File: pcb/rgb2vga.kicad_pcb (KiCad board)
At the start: 2 copper layers, 70.5 x 55.9 mm, 41 parts, among them J1 GPIO_0, J2 RGB_IN, J3 COCO3_RGB_IN, J4 C_VIDEO_IN, J5 GPIO_1, J6 VGA_OUT, J7 Conn_01x03_Male, SW1 SW_DIP_x10, SW2 SW_DP3T, U1 LM1881

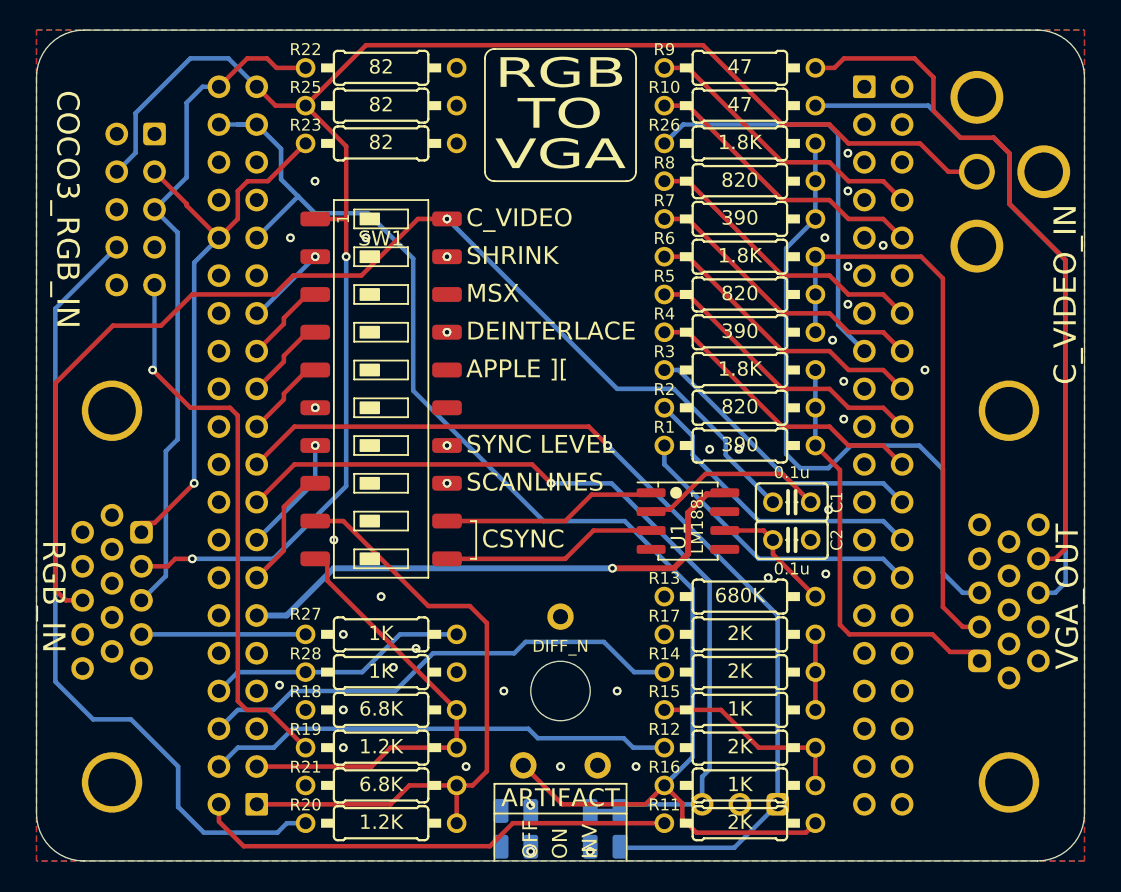
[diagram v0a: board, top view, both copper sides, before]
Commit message: multi-turn DAC trimmer pot
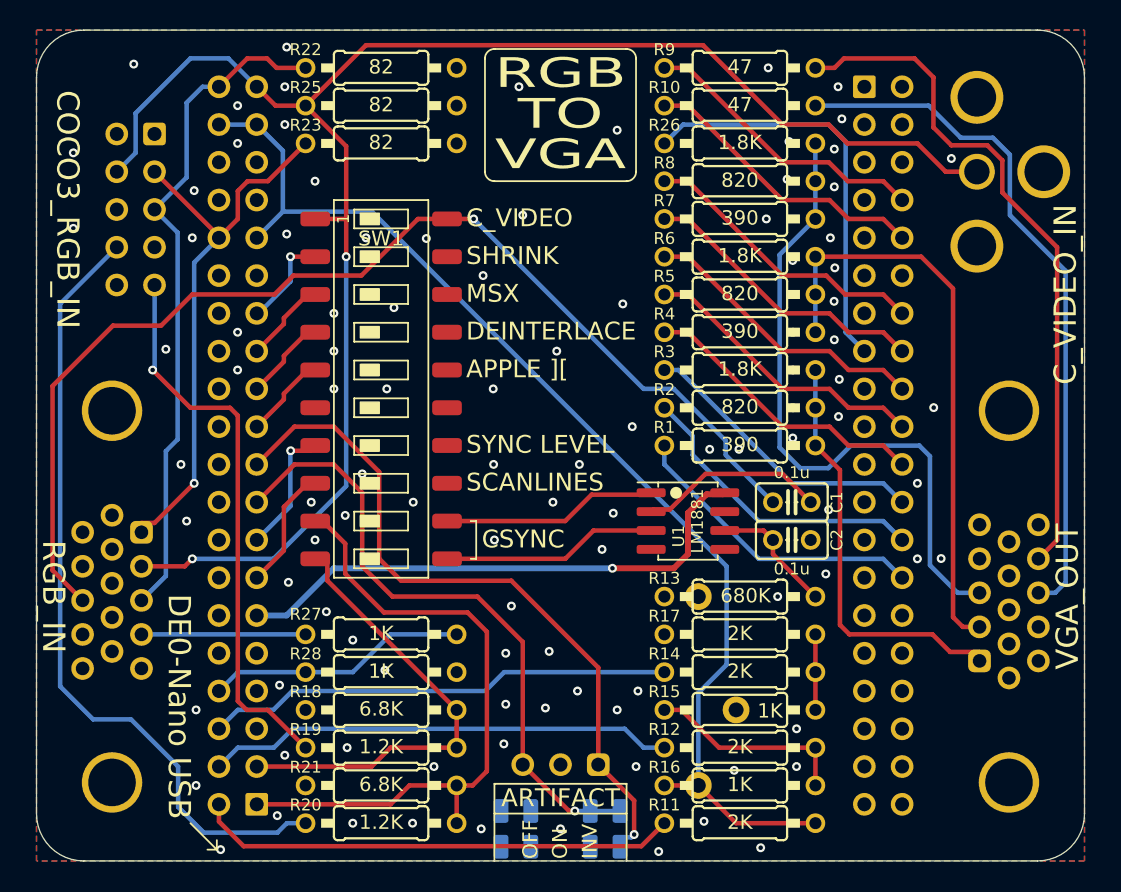
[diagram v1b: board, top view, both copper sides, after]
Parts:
- R24: footprint 000_LOCAL:PT10Lx-hole -> 000_LOCAL:Potentiometer_Bourns_3006P_Horizontal
- moved J7 12.4 mm to (145.7, 122.4)
- moved R24 11.2 mm to (152.5, 111.1), turned to 90 degrees
- renumbered REF** to DE0-Nano
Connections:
- J1 pad 10: (no net) -> unconnected-(J1-Pin_10-Pad10)
- J1 pad 14: (no net) -> unconnected-(J1-Pin_14-Pad14)
- J1 pad 16: (no net) -> unconnected-(J1-Pin_16-Pad16)
- J1 pad 18: (no net) -> unconnected-(J1-Pin_18-Pad18)
- J1 pad 20: (no net) -> unconnected-(J1-Pin_20-Pad20)
- J1 pad 22: (no net) -> unconnected-(J1-Pin_22-Pad22)
- J1 pad 24: (no net) -> unconnected-(J1-Pin_24-Pad24)
- J1 pad 26: (no net) -> unconnected-(J1-Pin_26-Pad26)
- J1 pad 28: (no net) -> unconnected-(J1-Pin_28-Pad28)
- J1 pad 29: (no net) -> unconnected-(J1-Pin_29-Pad29)
- J1 pad 33: (no net) -> unconnected-(J1-Pin_33-Pad33)
- J1 pad 34: (no net) -> unconnected-(J1-Pin_34-Pad34)
- J1 pad 35: (no net) -> unconnected-(J1-Pin_35-Pad35)
- J1 pad 36: (no net) -> unconnected-(J1-Pin_36-Pad36)
- J1 pad 5: (no net) -> unconnected-(J1-Pin_5-Pad5)
- J1 pad 7: (no net) -> unconnected-(J1-Pin_7-Pad7)
- J1 pad 9: (no net) -> unconnected-(J1-Pin_9-Pad9)
- J2 pad 11: (no net) -> unconnected-(J2-Pad11)
- J2 pad 12: (no net) -> unconnected-(J2-Pad12)
- J2 pad 14: (no net) -> unconnected-(J2-Pad14)
- J2 pad 15: (no net) -> unconnected-(J2-Pad15)
- J3 pad 6: (no net) -> unconnected-(J3-Pin_6-Pad6)
- J3 pad 7: (no net) -> unconnected-(J3-Pin_7-Pad7)
- J5 pad 1: (no net) -> unconnected-(J5-Pin_1-Pad1)
- J5 pad 11: (no net) -> unconnected-(J5-Pin_11-Pad11)
- J5 pad 13: (no net) -> unconnected-(J5-Pin_13-Pad13)
- J5 pad 17: (no net) -> unconnected-(J5-Pin_17-Pad17)
- J5 pad 19: (no net) -> unconnected-(J5-Pin_19-Pad19)
- J5 pad 2: (no net) -> unconnected-(J5-Pin_2-Pad2)
- J5 pad 21: (no net) -> unconnected-(J5-Pin_21-Pad21)
- J5 pad 23: (no net) -> unconnected-(J5-Pin_23-Pad23)
- J5 pad 25: (no net) -> unconnected-(J5-Pin_25-Pad25)
- J5 pad 27: (no net) -> unconnected-(J5-Pin_27-Pad27)
- J5 pad 29: (no net) -> unconnected-(J5-Pin_29-Pad29)
- J5 pad 3: (no net) -> unconnected-(J5-Pin_3-Pad3)
- J5 pad 31: (no net) -> unconnected-(J5-Pin_31-Pad31)
- J5 pad 32: (no net) -> unconnected-(J5-Pin_32-Pad32)
- J5 pad 33: (no net) -> unconnected-(J5-Pin_33-Pad33)
- J5 pad 34: (no net) -> unconnected-(J5-Pin_34-Pad34)
- J5 pad 35: (no net) -> unconnected-(J5-Pin_35-Pad35)
- J5 pad 36: (no net) -> unconnected-(J5-Pin_36-Pad36)
- J5 pad 37: (no net) -> unconnected-(J5-Pin_37-Pad37)
- J5 pad 38: (no net) -> unconnected-(J5-Pin_38-Pad38)
- J5 pad 39: (no net) -> unconnected-(J5-Pin_39-Pad39)
- J5 pad 4: (no net) -> unconnected-(J5-Pin_4-Pad4)
- J5 pad 40: (no net) -> unconnected-(J5-Pin_40-Pad40)
- J5 pad 5: (no net) -> unconnected-(J5-Pin_5-Pad5)
- J5 pad 6: (no net) -> unconnected-(J5-Pin_6-Pad6)
- J5 pad 7: (no net) -> unconnected-(J5-Pin_7-Pad7)
- J5 pad 9: (no net) -> unconnected-(J5-Pin_9-Pad9)
- J6 pad 11: (no net) -> unconnected-(J6-Pad11)
- J6 pad 12: (no net) -> unconnected-(J6-Pad12)
- J6 pad 15: (no net) -> unconnected-(J6-Pad15)
- J6 pad 4: (no net) -> unconnected-(J6-Pad4)
- R24 pad 1: (no net) -> GND
- U1 pad 5: (no net) -> unconnected-(U1-BURST-Pad5)
- U1 pad 7: (no net) -> unconnected-(U1-O/E-Pad7)
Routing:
- net /SW_ARTIF_INV: track 65.9 -> 48.0 mm
- net /DIFF_N: track 93.9 -> 78.1 mm
- net /SW_ARTIFACT: track 57.7 -> 42.9 mm
- net /D0: track 33.2 -> 31.5 mm
- net /VGA_V: track 47.5 -> 46.5 mm
- net /SW_SHRINK: track 5.51 -> 6.49 mm
- net /_HSYNC: track 43.3 -> 44.1 mm
- net /SW_SYNC_LVL: track 7.98 -> 8.74 mm
- net /VGA_B: track 43.9 -> 44.5 mm
- net /RGB_CS: track 77.3 -> 76.8 mm
- net GND: vias 39 -> 105
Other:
- board text added: "${COMMENT1} - ${REVISION} Based on FPGA RGB2VGA by Luis Antoniosi"
- board text added: "<-USB"
- board text added: "ARTIFACT SWITCH ON ENCLOSURE DP3T ON-OFF-ON"
- board text added: "DAC TRIM"
- board text added: "DE0-Nano USB"
- board text removed: "ARTIFACT SWITCH"
- board text removed: "Based on FPGA RGB2VGA by Luis Antoniosi"
- board text removed: "DIFF_N"
- board text removed: "DP3T ON-OFF-ON"
- board text removed: "ON ENCLOSURE"
- board text removed: "github.com/bkw777/rgb2vga - v010"

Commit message: SMT passives, add lowpass, decouple lm1881
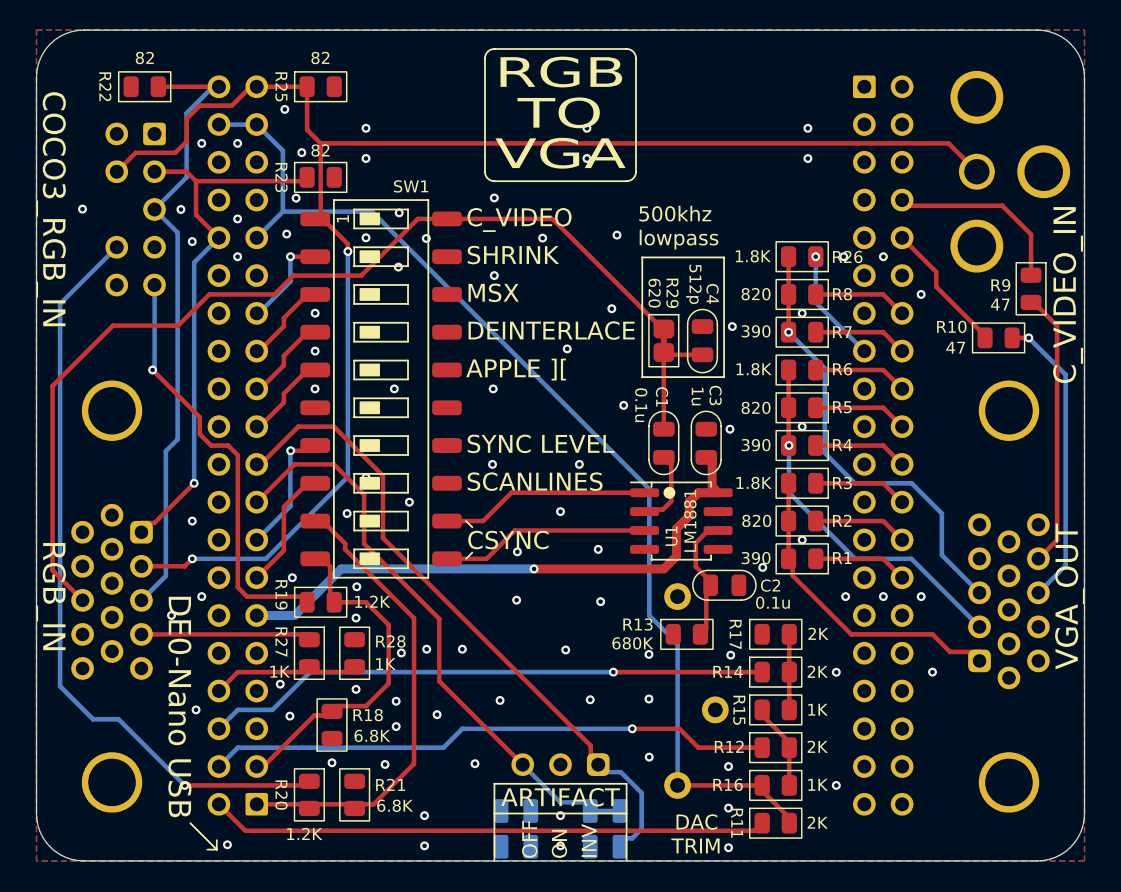
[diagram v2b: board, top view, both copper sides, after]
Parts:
- added C3: 1u, 000_LOCAL:C_0805, F.Cu at (153.0, 100.8)
- added C4: 512p, 000_LOCAL:C_0805, F.Cu at (152.7, 93.9)
- added R29: 620, 000_LOCAL:R_0805_SJC, F.Cu at (150.1, 93.9)
- C1, C2: footprint 000_LOCAL:C025-025X050 -> 000_LOCAL:C_0805
- J3: footprint 000_LOCAL:IDC-Header_2x05_P2.54mm_Horizontal -> 000_LOCAL:IDC-Header_2x05_P2.54mm_Horizontal COCO3 KEYED
- R1, R10, R11, R12, R13, R14, R15, R16, R17, R18, R19, R2, R20, R21, R22, R23, R25, R26, R27, R28, R3, R4, R5, R6, R7, R8, R9: footprint 000_LOCAL:0207_10 -> 000_LOCAL:R_0805
- moved R9 24.6 mm to (174.8, 90.4), turned to -90 degrees
- moved R10 23.4 mm to (172.7, 93.7)
- moved R22 15.9 mm to (115.2, 76.8), turned to 180 degrees
- moved R19 10.6 mm to (127.1, 111.5)
- moved C1 9.47 mm to (150.1, 100.8), turned to -90 degrees
- moved R3 8.70 mm to (159.4, 103.5), turned to 180 degrees
- moved R2 8.70 mm to (159.4, 106.0), turned to 180 degrees
- moved R26 8.70 mm to (159.4, 88.3), turned to 180 degrees
- moved R4 8.70 mm to (159.4, 101.0), turned to 180 degrees
- moved R6 8.70 mm to (159.4, 95.9), turned to 180 degrees
- moved R7 8.70 mm to (159.4, 93.3), turned to 180 degrees
- moved R8 8.70 mm to (159.4, 90.8), turned to 180 degrees
- moved R1 8.70 mm to (159.4, 108.6), turned to 180 degrees
- moved R5 8.70 mm to (159.4, 98.4), turned to 180 degrees
- moved C2 5.44 mm to (154.2, 110.4)
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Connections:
- C1 pad 1: /RGB_CS -> Net-(C1-Pad1)
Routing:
- net /VGA_V: track 46.5 -> 18.6 mm
- net /VGA_H: track 47.2 -> 20.0 mm, vias 0 -> 1
- net /B0: track 27.8 -> 7.70 mm, vias 0 -> 1
- net /VGA_G: track 39.4 -> 24.8 mm, vias 0 -> 1
- net /VGA_B: track 44.5 -> 30.2 mm, vias 0 -> 1
- net /R1: track 20.4 -> 6.33 mm
- net /R2: track 20.4 -> 6.33 mm
- net /G2: track 20.0 -> 6.33 mm
- net /G0: track 20.0 -> 6.33 mm
- net /B2: track 20.0 -> 6.33 mm
- net /B1: track 20.0 -> 6.33 mm
- net /G1: track 20.0 -> 6.33 mm
- net /R0: track 19.7 -> 6.33 mm
- net /RGB_CS: track 76.8 -> 64.1 mm, vias 1 -> 0
- net /_HSYNC: track 44.1 -> 31.5 mm
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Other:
- board text added: "${TITLE} - ${REVISION} ${COMMENT1} ${COMMENT2}"
- board text added: "500khz lowpass"
- board text removed: "${COMMENT1} - ${REVISION} Based on FPGA RGB2VGA by Luis Antoniosi"
